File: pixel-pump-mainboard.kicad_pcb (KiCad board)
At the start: 4 copper layers, 68 x 67.3 mm, 131 parts, among them J1 JST NC Valve, J10 BM10B-SRSS-TB(LF)(SN), J11 UART/SWD DNP, J12 TYPE-C-31-M-12, J2 JST NO Valve, J3 6P4C, J4 JST 3 Way Valve, J5 Jack-DC 12V, J6 Power Sw, J7 I2C, J8 SPI, J9 BM04B-SRSS-TBT(LF)(SN), Q1 BSS138, Q2 BSS138, Q3 BSS138, Q4 STN4NF20L, Q5 BSS138, SW1 BOOTSEL, U1 LD1117S33TR, U2 TPS62112RSAR, U3 W25Q128JVS, U4 RP2040, Y1 ABMM2-12.000MHZ-E2-T

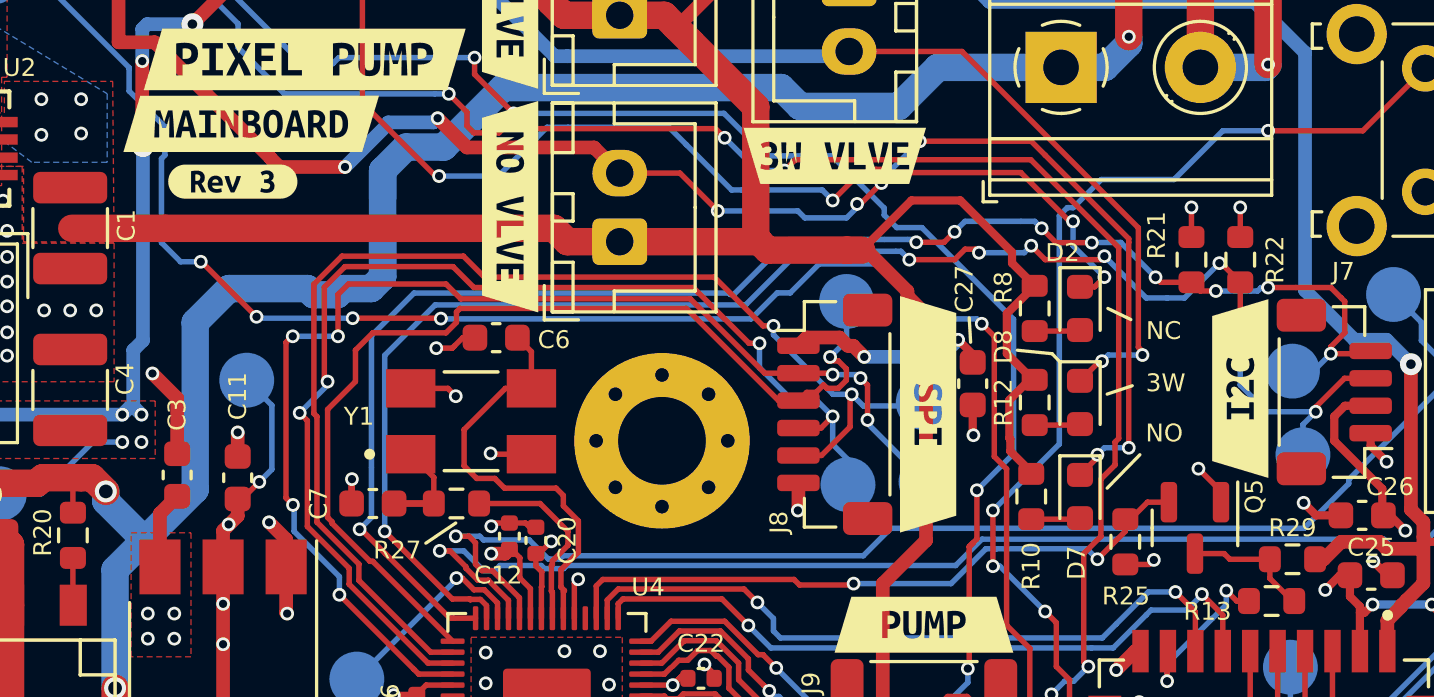
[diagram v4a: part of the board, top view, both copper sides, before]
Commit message: Rename ports to EXP1 and EXP2 and reduce mousebite stiffness
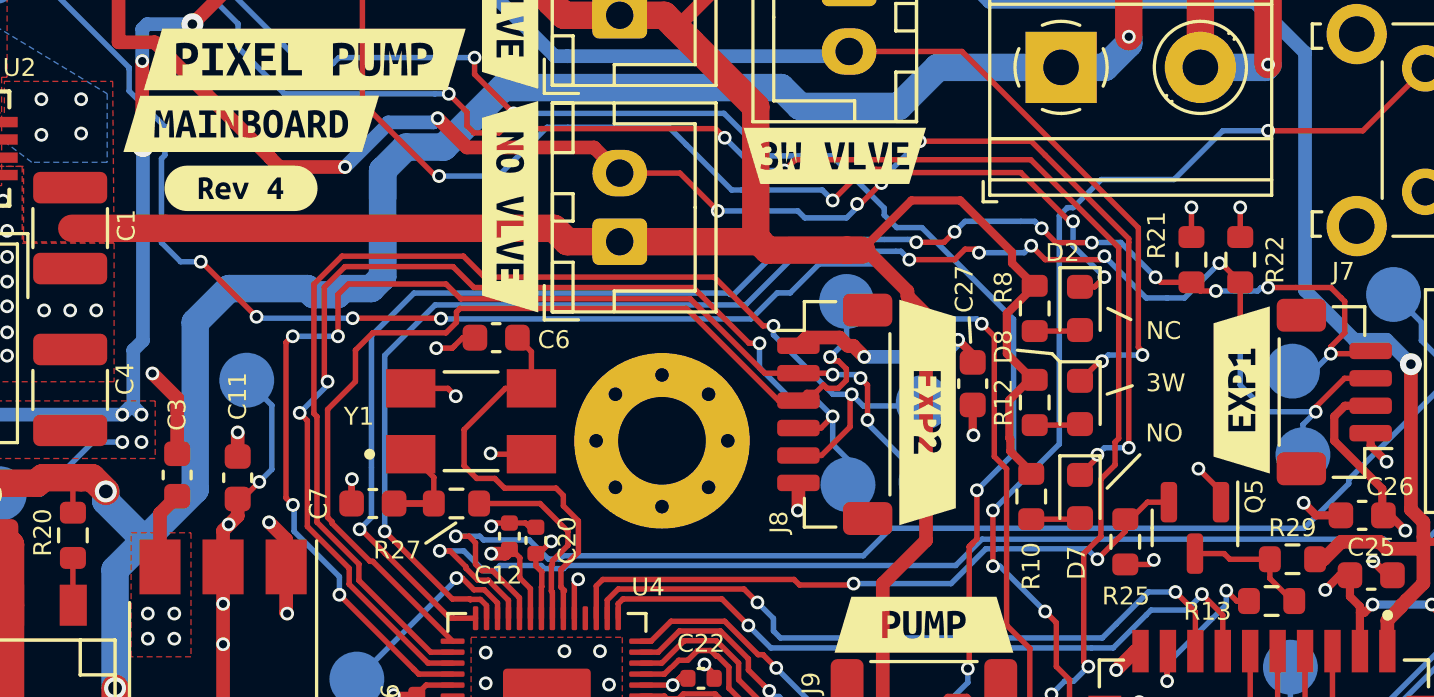
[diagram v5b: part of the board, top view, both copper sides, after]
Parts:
- removed kibuzzard-6107E29B: G***, kibuzzard-6107E29B
- removed kibuzzard-6107E2CE: G***, kibuzzard-6107E2CE
- removed kibuzzard-61DF0B83: G***, kibuzzard-61DF0B83
- added kibuzzard-626BB8E0: G***, kibuzzard-626BB8E0, F.Cu at (121.2, 125.4)
- added kibuzzard-626BB906: G***, kibuzzard-626BB906, F.Cu at (109.8, 126.2)
- added kibuzzard-626BB945: G***, kibuzzard-626BB945, F.Cu at (84.7, 118.0)
- J7: value I2C -> EXP1
- J8: value SPI -> EXP2

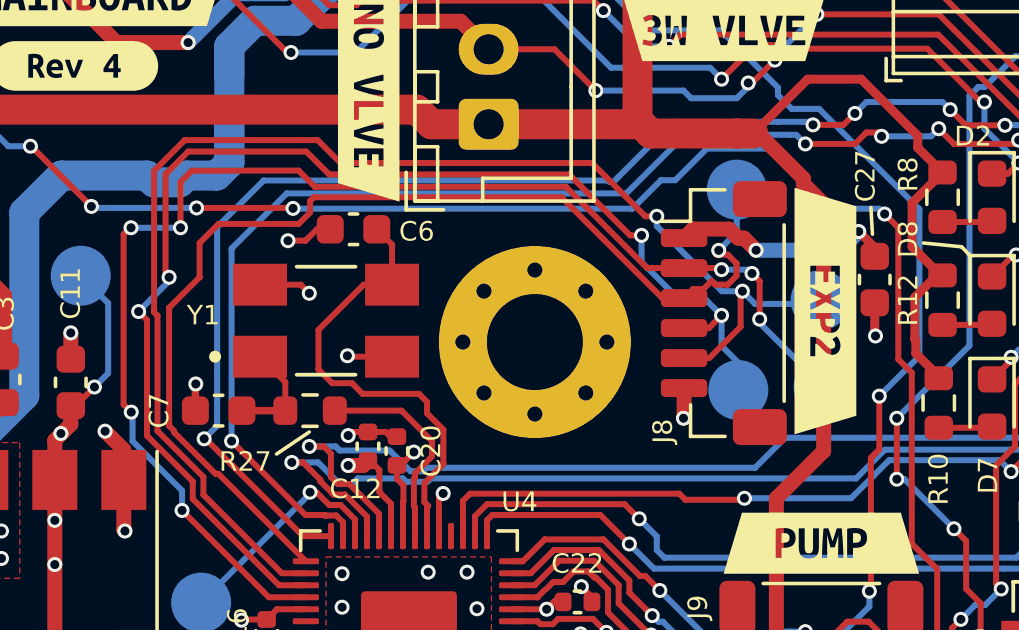
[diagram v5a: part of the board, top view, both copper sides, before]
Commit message: Switch to CTS 445C25D12M00000 12 MHz crystal
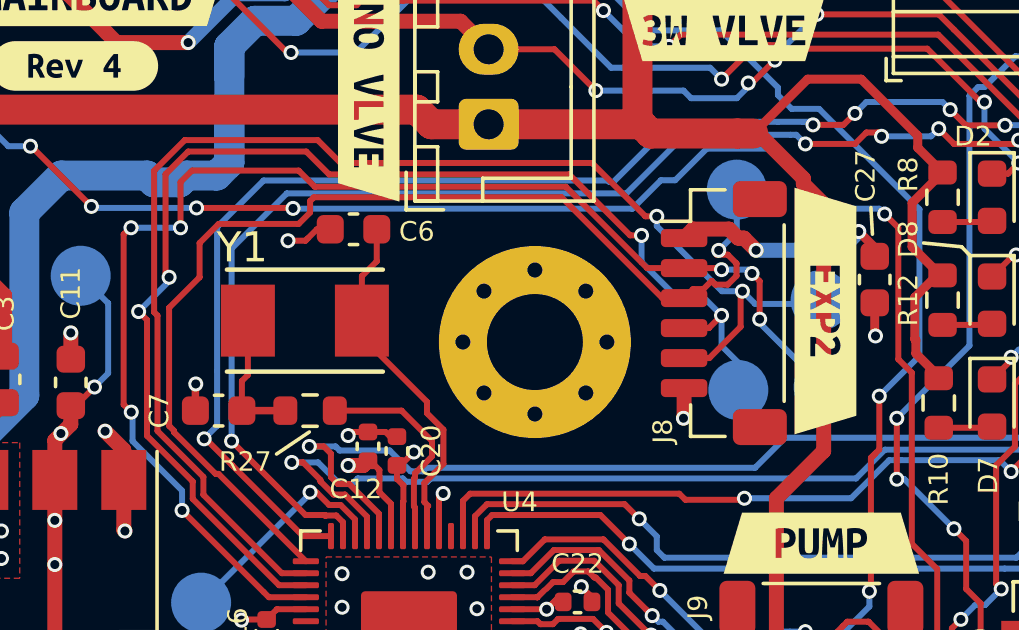
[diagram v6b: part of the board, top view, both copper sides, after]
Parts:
- Y1: value ABMM2-12.000MHZ-E2-T -> 445C25D12M00000; footprint ABMM2-12:XTAL_ABMM2-12.000MHZ-E2-T -> CTS 445C25D12M00000 12MHz:CTS-445-0-0-0
- moved Y1 0.71 mm to (92.4, 126.5)
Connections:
- Y1 pad 2: GND -> OSC_IN
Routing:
- net OSC_IN: track 15.6 -> 11.9 mm
- net GND: track 62.8 -> 59.6 mm, vias 94 -> 92
- net Net-(C7-Pad1): track 3.59 -> 4.53 mm

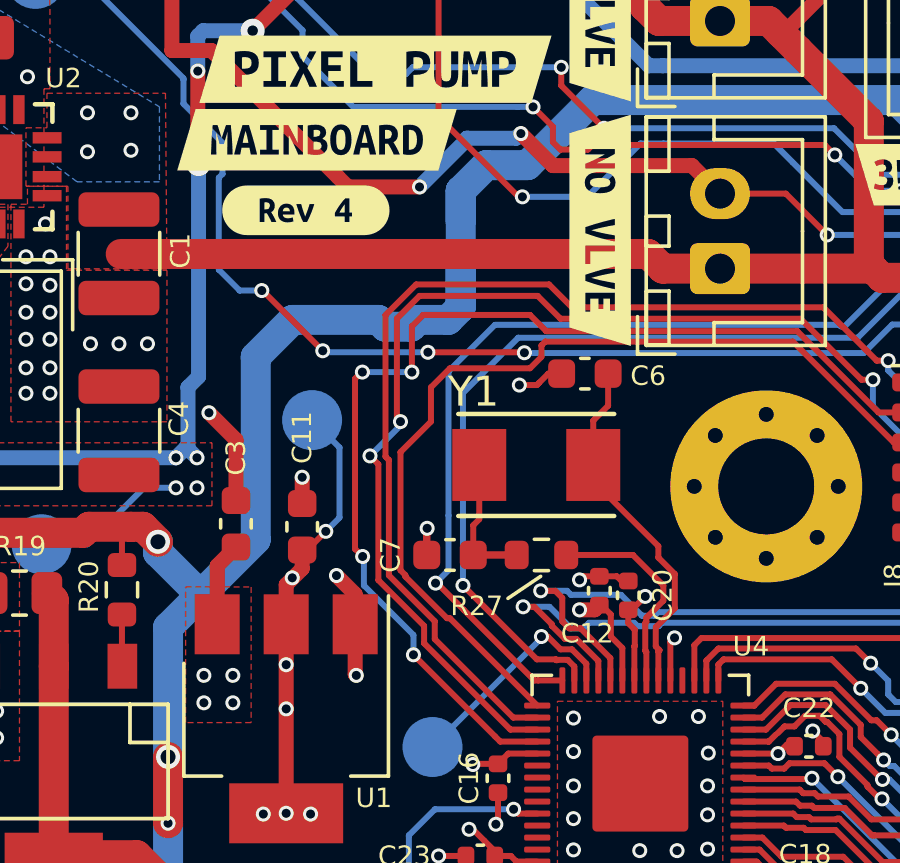
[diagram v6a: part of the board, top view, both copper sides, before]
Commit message: Revert back to ABM12 footprint
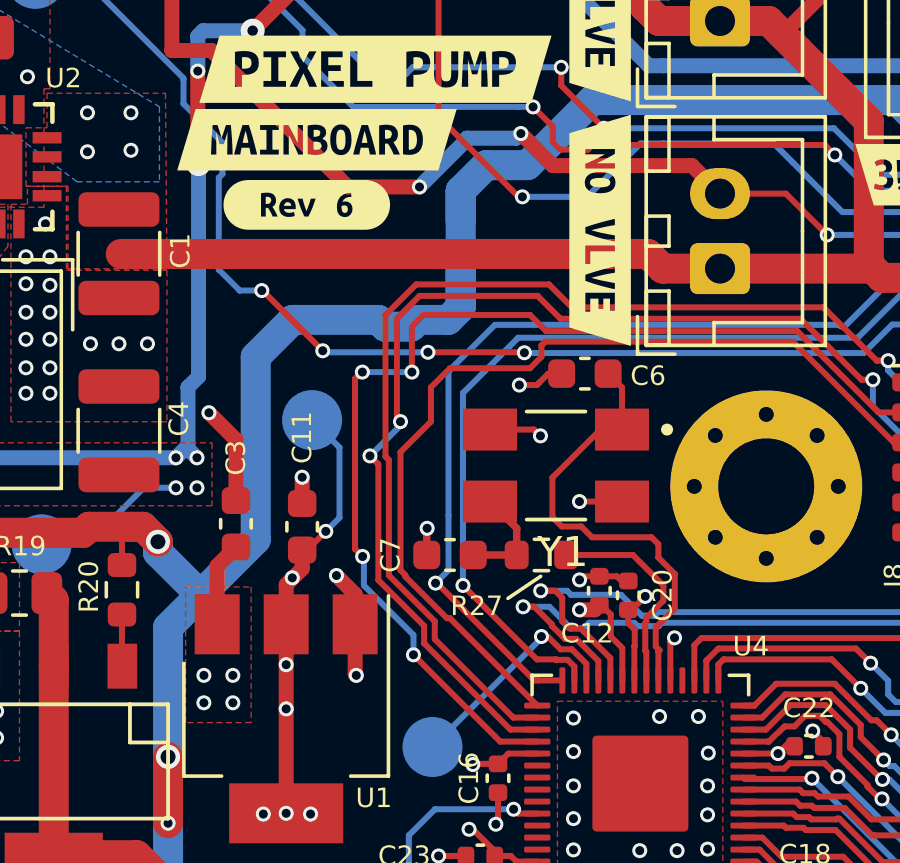
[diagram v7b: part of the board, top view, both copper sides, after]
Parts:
- removed kibuzzard-626BB945: G***, kibuzzard-626BB945
- added kibuzzard-62DE7A3F: G***, kibuzzard-62DE7A3F, F.Cu at (84.8, 117.9)
- Y1: value 445C25D12M00000 -> ABMM2-12.000MHZ-E2-T; footprint CTS 445C25D12M00000 12MHz:CTS-445-0-0-0 -> ABMM2-12:XTAL_ABMM2-12.000MHZ-E2-T
- moved Y1 0.66 mm to (93.1, 126.6), turned to 180 degrees
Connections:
- Y1 pad 1: Net-(C7-Pad1) -> OSC_IN
- Y1 pad 2: OSC_IN -> GND
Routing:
- net OSC_IN: track 11.9 -> 15.4 mm
- net GND: track 59.6 -> 62.8 mm, vias 92 -> 94
- net Net-(C7-Pad1): track 4.53 -> 3.60 mm

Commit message: Assign all MPNs
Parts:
- removed kibuzzard-62DE7A3F: G***, kibuzzard-62DE7A3F
- C4: value 22u 10V -> 22u 16V
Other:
- board text added: "Rev 7"
- board text added: "by Robin Reiter Hergatz, DE Aug 2022"
- board text removed: "by Robin Reiter Hergatz, DE Aug 2021"
